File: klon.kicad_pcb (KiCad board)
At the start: 2 copper layers, 62 x 83 mm, 71 parts, among them SW1 SW_DPDT_x2, U1 TL072, U2 LTC1044, U3 TL072

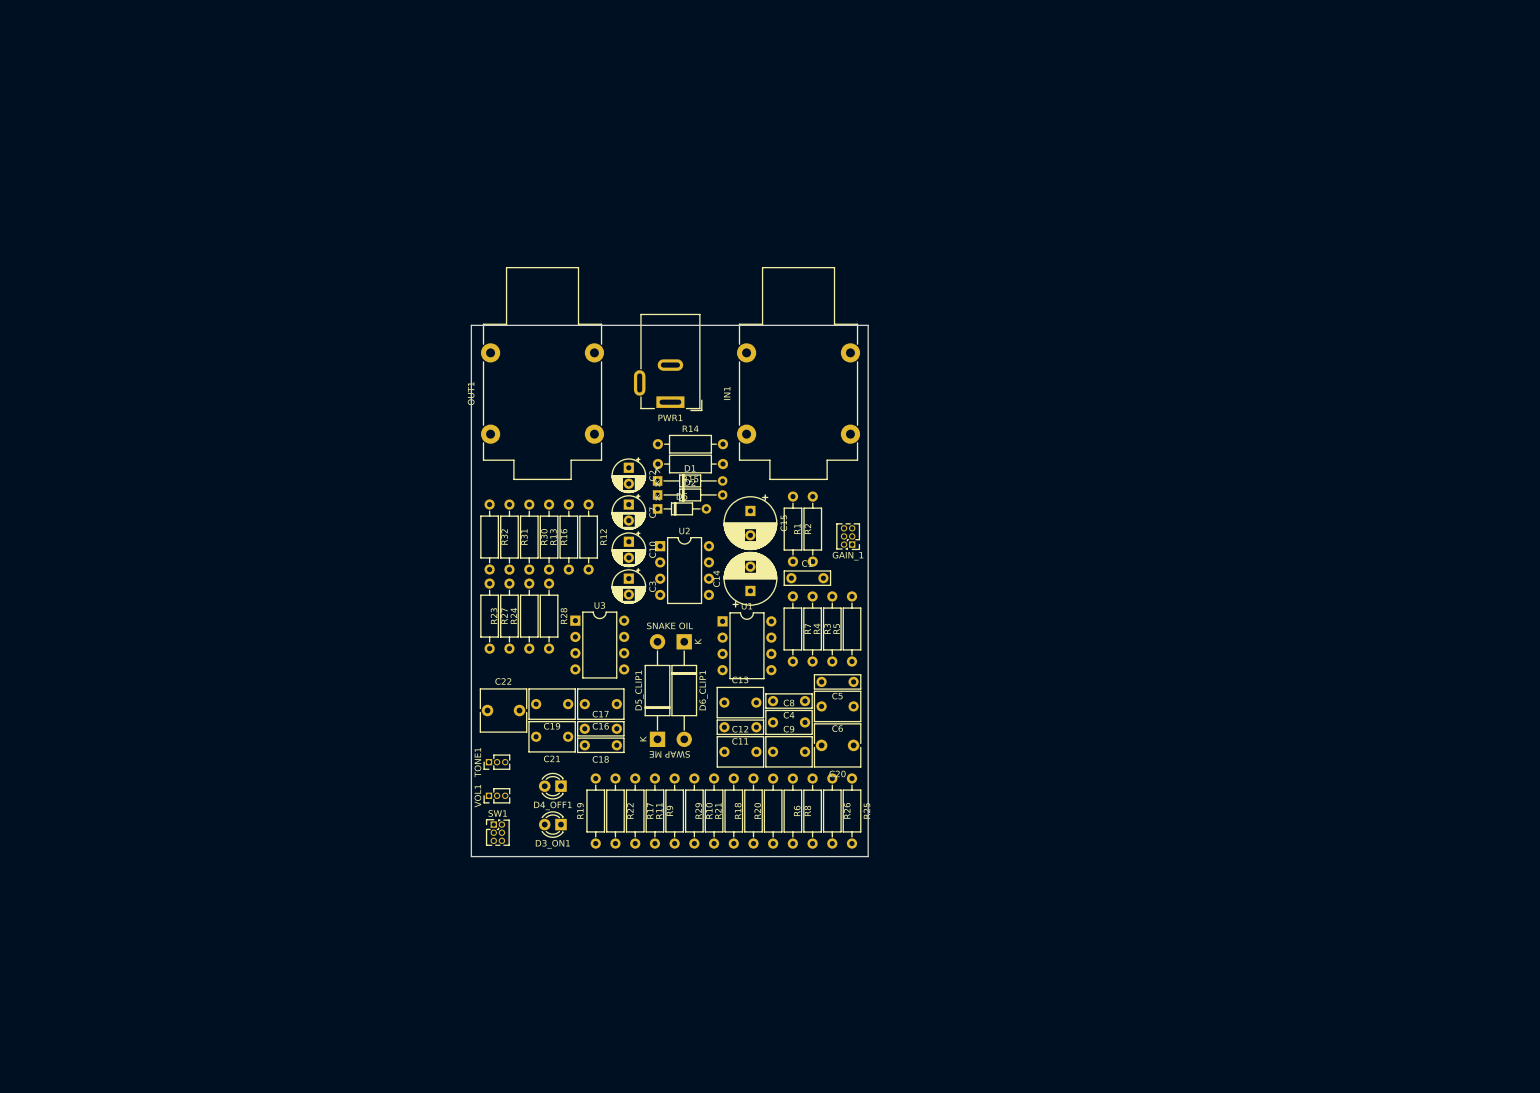
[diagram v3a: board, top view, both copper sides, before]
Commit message: add custom models, change pcb board layout
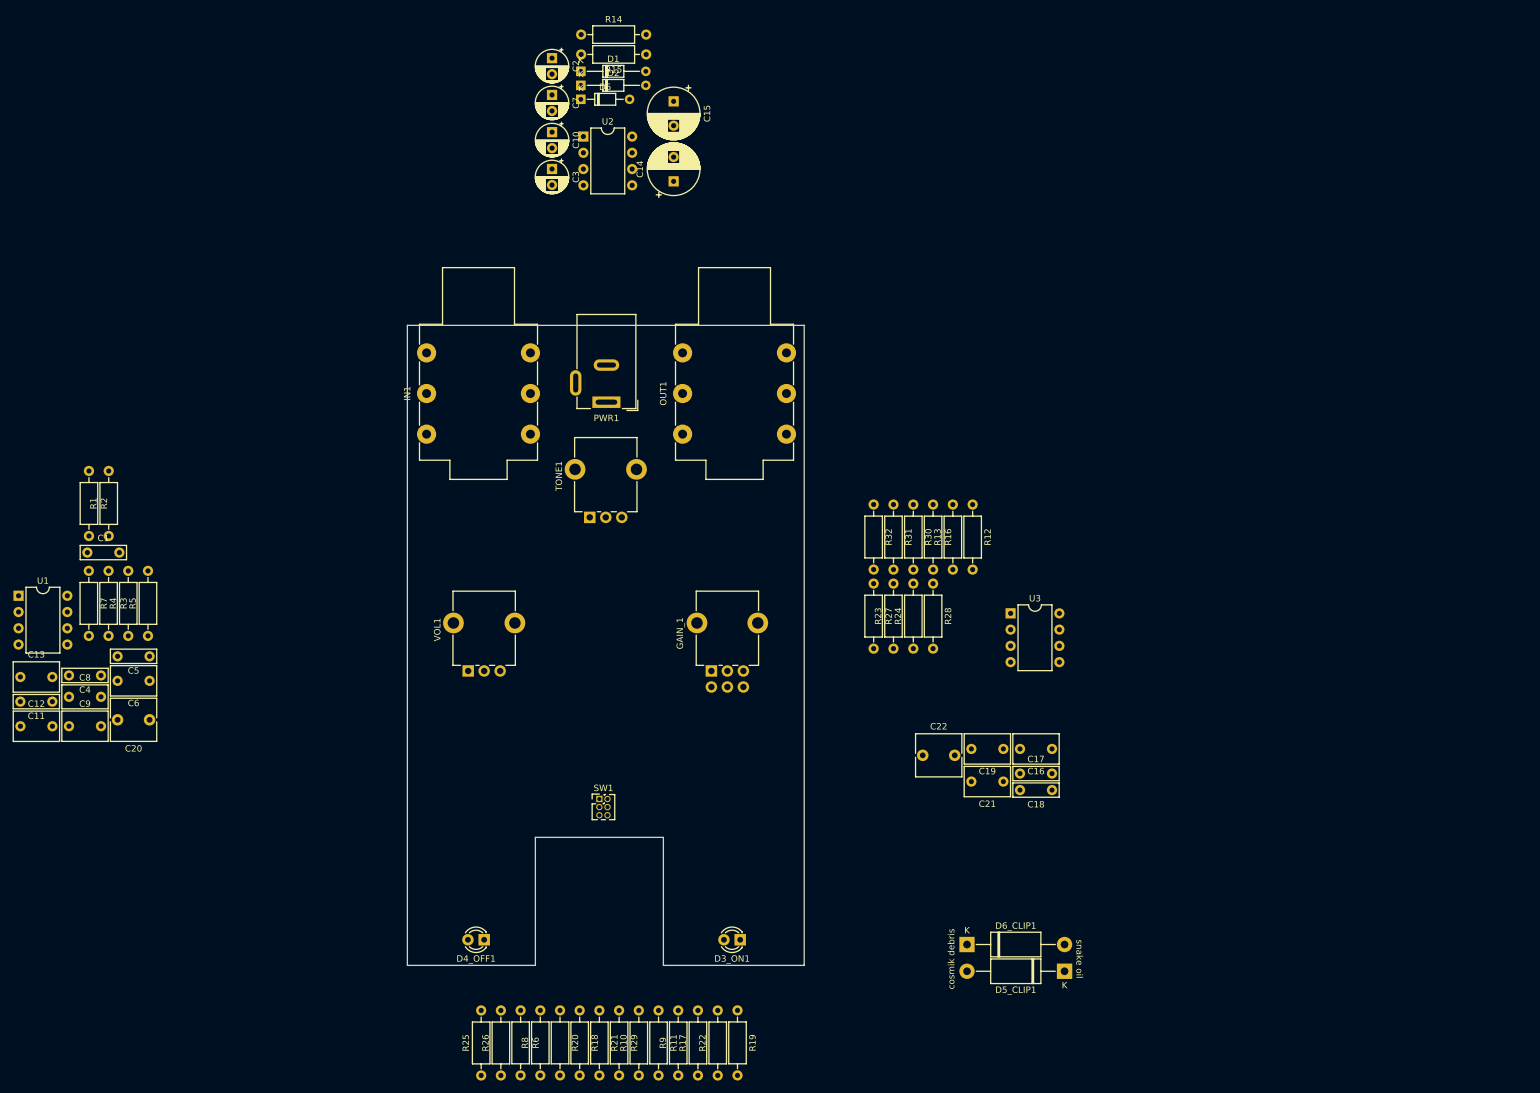
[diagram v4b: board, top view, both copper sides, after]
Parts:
- GAIN_1: footprint Connector_PinHeader_1.27mm:PinHeader_2x03_P1.27mm_Vertical -> Potentiometer_THT:Potentiometer_Alpha_RD902F-40-00D_Dual_Vertical_CircularHoles
- IN1, OUT1: value AudioJack2 -> AudioJack3; footprint Connector_Audio:Jack_6.35mm_Neutrik_NMJ4HFD2_Horizontal -> Connector_Audio:Jack_6.35mm_Neutrik_NMJ6HFD2_Horizontal
- TONE1, VOL1: footprint Connector_PinHeader_1.27mm:PinHeader_1x03_P1.27mm_Vertical -> Potentiometer_THT:Potentiometer_Alpha_RD901F-40-00D_Single_Vertical_CircularHoles
- moved C1 110.1 mm to (-10.0, 75.5)
- moved C11 110.1 mm to (-15.5, 98.8)
- moved C12 110.1 mm to (-20.5, 102.6)
- moved C13 110.1 mm to (-20.5, 94.9)
- moved C20 110.1 mm to (-0.28, 101.6)
- moved C4 110.1 mm to (-7.87, 94.7)
- moved C5 110.1 mm to (-0.28, 91.7)
- moved C6 110.1 mm to (-0.28, 95.5)
- moved C8 110.1 mm to (-12.9, 98.0)
- moved C9 110.1 mm to (-12.9, 102.6)
- moved R1 110.1 mm to (-6.66, 72.9)
- moved R2 110.1 mm to (-9.75, 62.8)
- moved R3 110.1 mm to (-6.69, 78.4)
- moved R4 110.1 mm to (-3.61, 88.5)
- moved R5 110.1 mm to (-0.53, 88.5)
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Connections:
- OUT1 pad S: Net-(OUT1-PadS) -> Net-(OUT1-PadR)
- R32 pad 1: Net-(OUT1-PadS) -> Net-(OUT1-PadR)
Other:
- board size 62 x 83 mm -> 62 x 100 mm
- board text added: "cosmik debris"
- board text added: "snake oil"
- board text removed: "SNAKE OIL"
- board text removed: "SWAP ME"

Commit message: optimize board to new dimensions
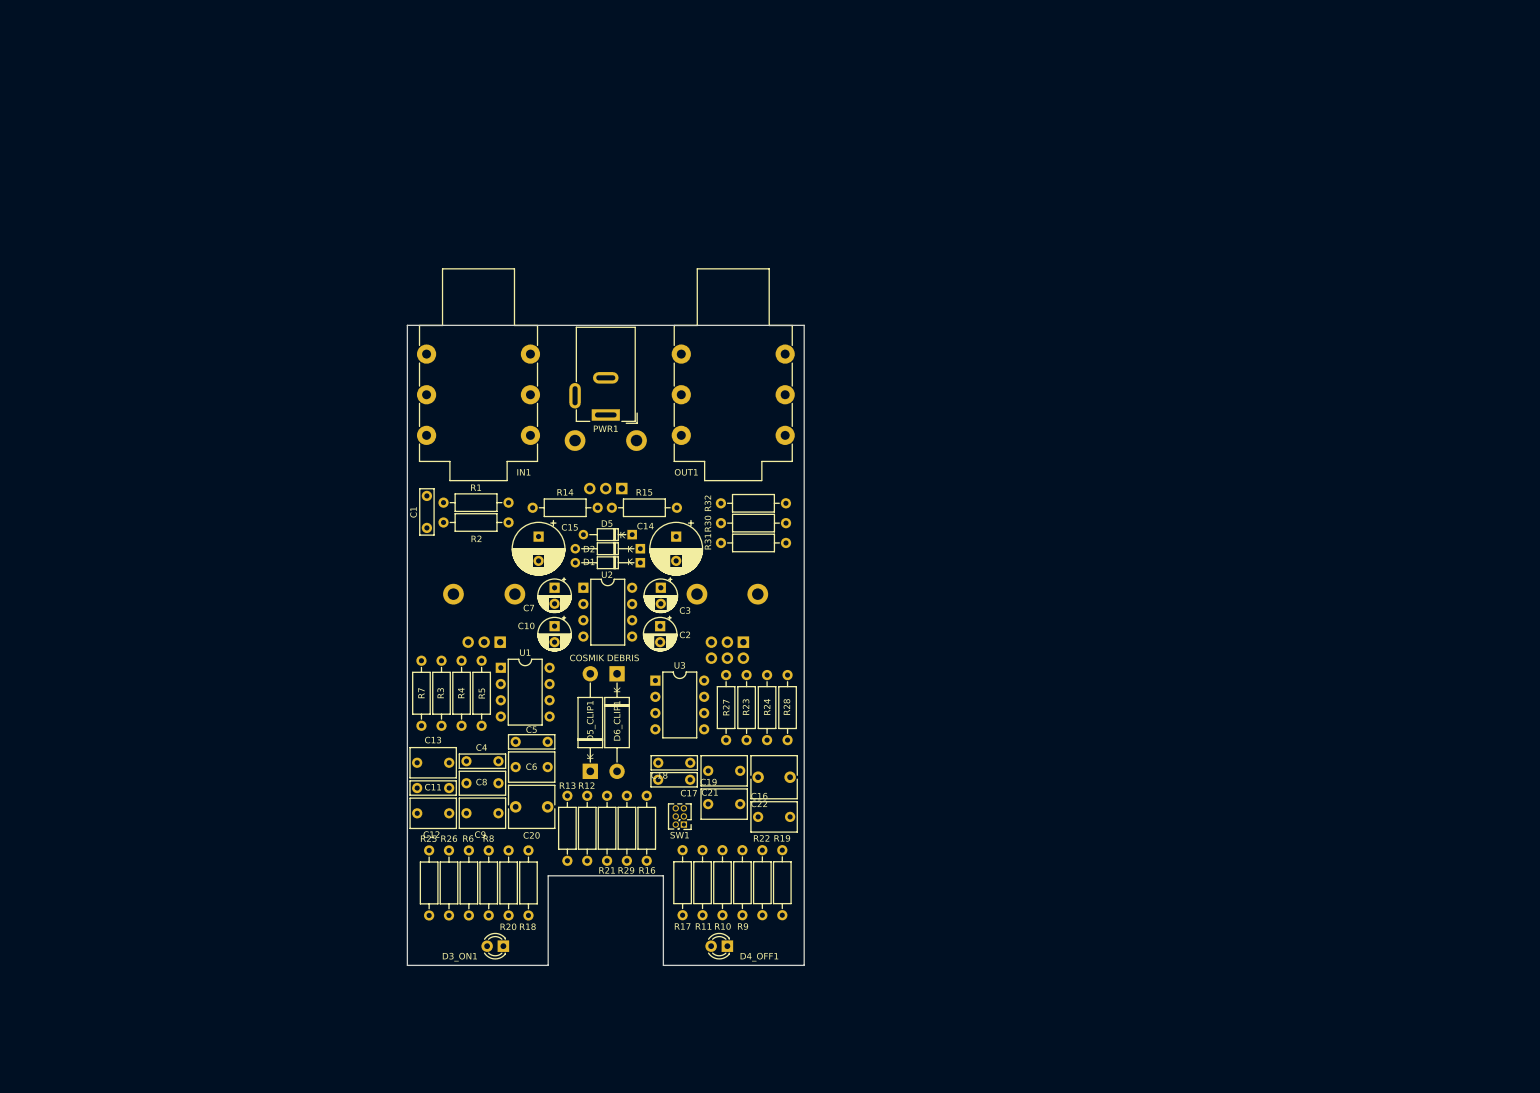
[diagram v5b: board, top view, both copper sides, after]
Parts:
- GAIN_1, TONE1, VOL1: moved to B.Cu
- moved C2 90.3 mm to (79.5, 87.0)
- moved R12 82.0 mm to (68.1, 123.7), turned to 90 degrees
- moved D5_CLIP1 80.4 mm to (68.6, 109.7), turned to 90 degrees
- moved D1 77.3 mm to (76.4, 77.1), turned to 180 degrees
- moved C10 77.2 mm to (63.0, 87.0)
- moved C7 77.0 mm to (63.0, 81.0)
- moved U1 76.2 mm to (54.6, 93.5)
- moved R14 74.3 mm to (59.6, 68.5)
- moved D2 73.0 mm to (76.4, 74.9), turned to 180 degrees
- moved C15 71.2 mm to (60.5, 73.0)
- moved R15 71.0 mm to (72.0, 68.5), turned to 0 degrees
- moved U2 70.5 mm to (67.5, 81.0)
- moved R13 69.8 mm to (65.0, 113.5), turned to 270 degrees
- moved D6_CLIP1 69.1 mm to (72.8, 94.4), turned to 270 degrees
- moved D5 68.5 mm to (75.1, 72.7), turned to 180 degrees
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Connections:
- U1 pad 1: Net-(C12-Pad1) -> Net-(C20-Pad1)
- U1 pad 2: Net-(C8-Pad1) -> Net-(C20-Pad1)
- U1 pad 3: Net-(C11-Pad1) -> Net-(C1-Pad1)
- U1 pad 5: Net-(C20-Pad1) -> Net-(C8-Pad1)
- U1 pad 6: Net-(C1-Pad1) -> Net-(C11-Pad1)
- U1 pad 7: Net-(C20-Pad1) -> Net-(C12-Pad1)
- U2 pad 6: (no net) -> Net-(U2-Pad6)
- U2 pad 7: (no net) -> Net-(U2-Pad7)
- U3 pad 1: Net-(C22-Pad2) -> Net-(C19-Pad1)
- U3 pad 2: Net-(C21-Pad1) -> Net-(C18-Pad1)
- U3 pad 6: Net-(C18-Pad1) -> Net-(C21-Pad1)
- U3 pad 7: Net-(C19-Pad1) -> Net-(C22-Pad2)
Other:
- outline, holes or cut-outs redrawn
- board text added: "COSMIK DEBRIS"
- board text removed: "cosmik debris"
- board text removed: "snake oil"

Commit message: add pcb traces
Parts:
- moved C12 20.9 mm to (62.4, 117.5), turned to 180 degrees
- moved C13 15.9 mm to (57.3, 110.1)
- moved C20 15.0 mm to (46.9, 116.4)
- moved C5 15.0 mm to (46.9, 106.3)
- moved C6 15.0 mm to (46.9, 110.2)
- moved C11 12.4 mm to (57.3, 106.2), turned to 0 degrees
- moved R4 11.6 mm to (42.2, 102.2), turned to 90 degrees
- moved R5 11.6 mm to (45.4, 102.2), turned to 90 degrees
- moved R3 11.0 mm to (48.6, 92.0), turned to 270 degrees
- moved R7 9.61 mm to (51.8, 102.2)
- moved R28 9.60 mm to (89.8, 105.0)
- moved R23 6.40 mm to (99.4, 94.8)
- moved C8 4.56 mm to (49.6, 107.0)
- moved R27 3.20 mm to (93.0, 105.0)
- moved C4 2.33 mm to (54.6, 110.4)
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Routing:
- net +9V: track 0.00 -> 204.4 mm
- net Net-(C5-Pad2): track 0.00 -> 174.6 mm
- net Net-(C8-Pad1): track 0.00 -> 171.1 mm, vias 0 -> 1
- net Net-(R26-Pad1): track 0.00 -> 164.0 mm, vias 0 -> 1
- net Net-(OUT1-PadT): track 0.00 -> 140.6 mm
- net Net-(R30-Pad2): track 0.00 -> 134.1 mm
- net /+4.5V: track 0.00 -> 123.0 mm
- net Net-(GAIN_1-Pad2): track 0.00 -> 121.6 mm
- net Net-(C18-Pad1): track 0.00 -> 110.2 mm
- net Net-(C16-Pad2): track 0.00 -> 73.9 mm, vias 0 -> 1
- net Net-(C11-Pad1): track 0.00 -> 64.2 mm
- net Net-(R23-Pad1): track 0.00 -> 58.0 mm
- net Net-(C21-Pad2): track 0.00 -> 56.8 mm, vias 0 -> 1
- net Net-(C12-Pad1): track 0.00 -> 49.5 mm
- net Net-(C21-Pad1): track 0.00 -> 48.6 mm
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- added copper zone on B.Cu, net GND
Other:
- board text added: "v0.0.1"

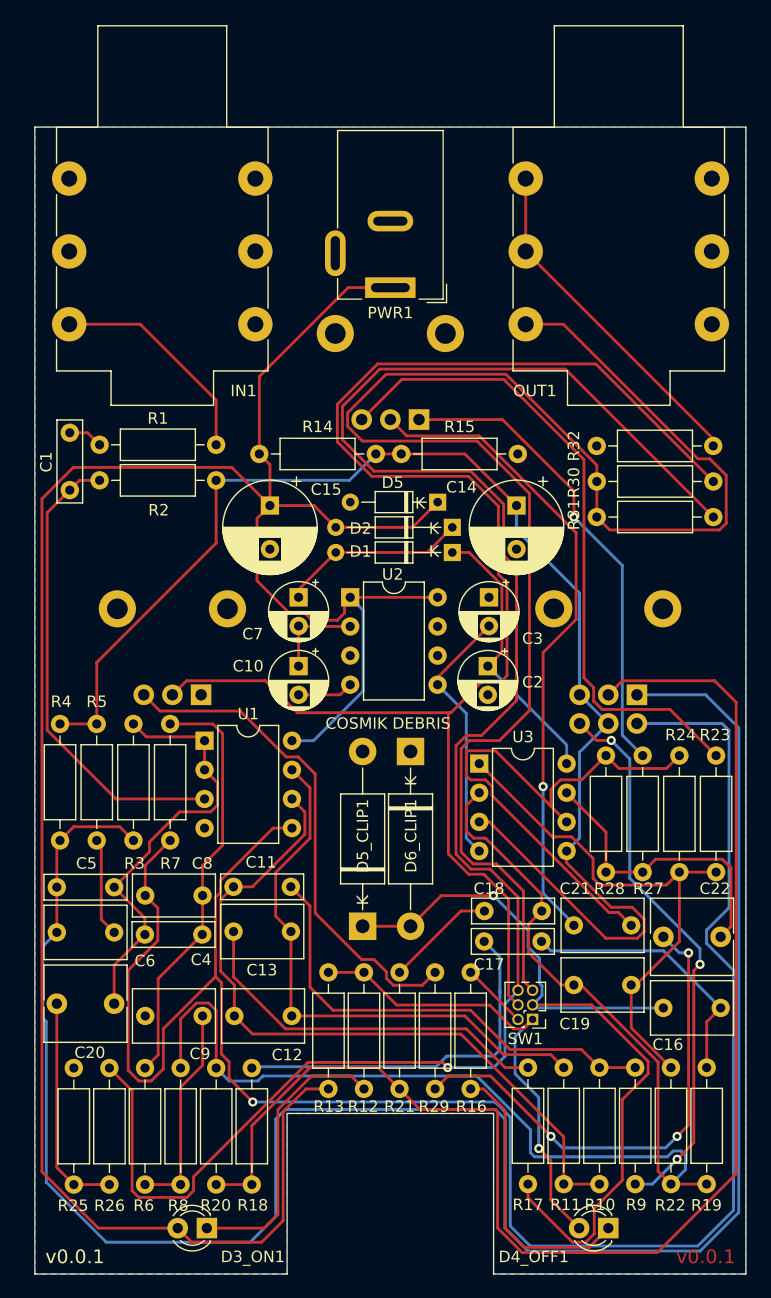
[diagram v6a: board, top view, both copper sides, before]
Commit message: fix power polarity, new PCB layout
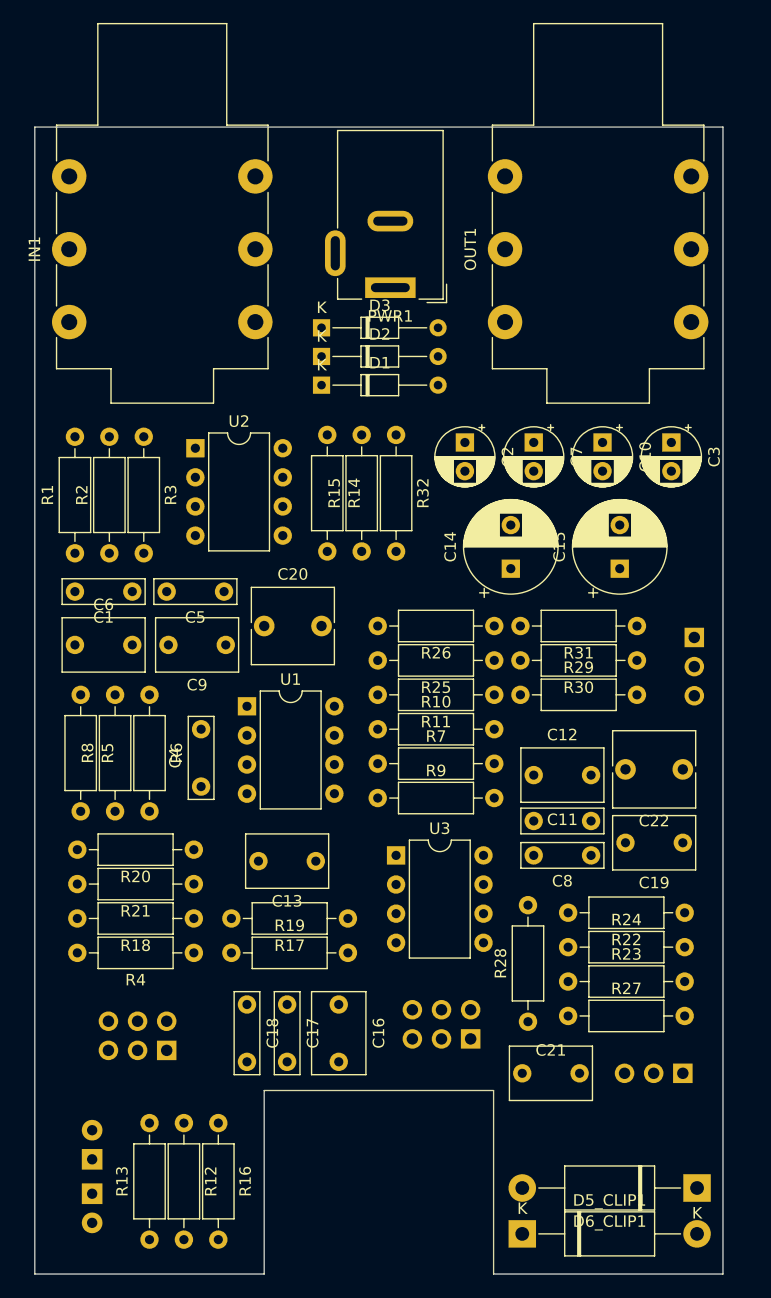
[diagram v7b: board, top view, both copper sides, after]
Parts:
- removed D5: 1N4742, Diode_THT:D_DO-34_SOD68_P7.62mm_Horizontal
- added D3: 1N4742, Diode_THT:D_DO-34_SOD68_P10.16mm_Horizontal, F.Cu at (65.0, 57.5)
- C8: footprint Capacitor_THT:C_Rect_L7.0mm_W3.5mm_P5.00mm -> Capacitor_THT:C_Rect_L7.0mm_W2.0mm_P5.00mm
- D3_ON1, D4_OFF1: moved to B.Cu
- GAIN_1: footprint Potentiometer_THT:Potentiometer_Alpha_RD902F-40-00D_Dual_Vertical_CircularHoles -> Connector_PinHeader_2.54mm:PinHeader_2x03_P2.54mm_Vertical
- SW1: footprint Connector_PinHeader_1.27mm:PinHeader_2x03_P1.27mm_Vertical -> Connector_PinHeader_2.54mm:PinHeader_2x03_P2.54mm_Vertical; moved to B.Cu
- TONE1, VOL1: footprint Potentiometer_THT:Potentiometer_Alpha_RD901F-40-00D_Single_Vertical_CircularHoles -> Connector_PinHeader_2.54mm:PinHeader_1x03_P2.54mm_Vertical
- moved TONE1 61.5 mm to (96.5, 122.5)
- moved GAIN_1 51.4 mm to (51.5, 120.5)
- moved R26 51.1 mm to (80.1, 83.5), turned to 180 degrees
- moved R25 51.1 mm to (80.1, 86.5), turned to 180 degrees
- moved R19 46.1 mm to (57.1, 112.0), turned to 0 degrees
- moved D6_CLIP1 45.5 mm to (97.7, 132.5), turned to 180 degrees
- moved D4_OFF1 45.1 mm to (45.0, 133.0), turned to 270 degrees
- moved R10 44.1 mm to (69.9, 92.5), turned to 0 degrees
- moved VOL1 43.3 mm to (97.5, 84.5), turned to 180 degrees
- moved R6 42.7 mm to (50.0, 89.5), turned to 270 degrees
- moved R9 40.5 mm to (69.9, 98.5), turned to 0 degrees
- moved C8 39.0 mm to (88.5, 103.5), turned to 180 degrees
- moved C20 35.4 mm to (60.0, 83.5), turned to 0 degrees
- moved C16 33.3 mm to (66.5, 116.5), turned to 270 degrees
- moved C9 33.1 mm to (56.6, 85.2), turned to 180 degrees
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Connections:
- PWR1 pad 1: +9V -> GND
- PWR1 pad 2: GND -> +9V
- SW1 pad 1: Net-(D4_OFF1-Pad2) -> Net-(C16-Pad2)
- SW1 pad 3: Net-(C16-Pad2) -> Net-(D4_OFF1-Pad2)
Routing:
- net +9V: track 204.4 -> 0.00 mm
- net Net-(C5-Pad2): track 174.6 -> 0.00 mm
- net Net-(C8-Pad1): track 171.1 -> 0.00 mm, vias 1 -> 0
- net Net-(R26-Pad1): track 164.0 -> 0.00 mm, vias 1 -> 0
- net Net-(OUT1-PadT): track 140.6 -> 0.00 mm
- net Net-(R30-Pad2): track 134.1 -> 0.00 mm
- net /+4.5V: track 123.0 -> 0.00 mm
- net Net-(GAIN_1-Pad2): track 121.6 -> 0.00 mm
- net Net-(C18-Pad1): track 110.2 -> 0.00 mm
- net Net-(C16-Pad2): track 73.9 -> 0.00 mm, vias 1 -> 0
- net Net-(C11-Pad1): track 64.2 -> 0.00 mm
- net Net-(R23-Pad1): track 58.0 -> 0.00 mm
- net Net-(C21-Pad2): track 56.8 -> 0.00 mm, vias 1 -> 0
- net Net-(C12-Pad1): track 49.5 -> 0.00 mm
- net Net-(C21-Pad1): track 48.6 -> 0.00 mm
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- removed copper zone on B.Cu, net GND
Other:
- board size 62 x 100 mm -> 60 x 100 mm
- board text removed: "COSMIK DEBRIS"
- board text removed: "v0.0.1"
